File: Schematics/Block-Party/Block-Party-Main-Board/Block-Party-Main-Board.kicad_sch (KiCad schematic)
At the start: 28 parts, among them U1 ESP32-S3-DEVKITC-1-N8R2

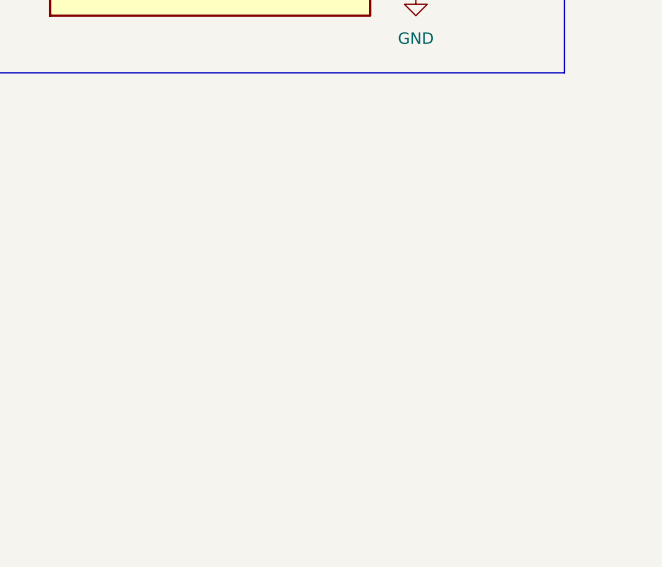
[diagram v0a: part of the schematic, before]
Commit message: Added a usb power connector.
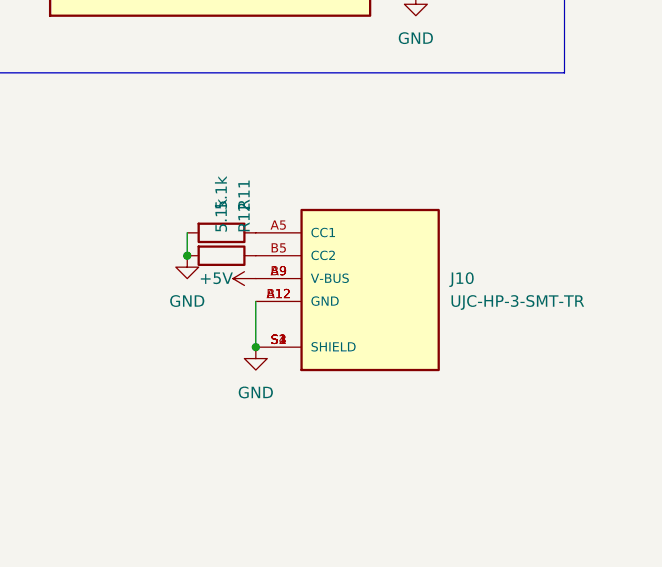
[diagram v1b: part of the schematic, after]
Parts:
- added J10: UJC-HP-3-SMT-TR, UJC-HP-3-SMT-TR:CUI_UJC-HP-3-SMT-TR, symbol UJC-HP-3-SMT-TR:UJC-HP-3-SMT-TR
- added R11, R12: 5.1k, Resistor_SMD:R_0805_2012Metric, symbol Device:R
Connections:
- net +5V: now also J10.A9 (V-BUS), J10.B9 (V-BUS)
- net GND: now also J10.A12 (GND), J10.B12 (GND), J10.S1 (SHIELD), J10.S2 (SHIELD), J10.S3 (SHIELD), J10.S4 (SHIELD), R11.2, R12.2
- new net: J10.A5 (CC1), R11.1
- new net: J10.B5 (CC2), R12.1
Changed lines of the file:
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@@
     (company "Block Party")
+  )
+  (junction (at 193.04 135.89) (diameter 0) (color 0 0 0 0)
+  )
+  (junction (at 185.42 125.73) (diameter 0) (color 0 0 0 0)
   )
   (no_connect (at 165.1 50.8))
@@
     (stroke (width 0) (type default))
   )
+  (wire (pts (xy 185.42 123.19) (xy 185.42 125.73))
+    (stroke (width 0) (type default))
+  )
+  (wire (pts (xy 193.04 130.81) (xy 193.04 135.89))
+    (stroke (width 0) (type default))
+  )
   (rectangle (start 62.23 97.79) (end 140.97 171.45)
     (stroke (width 0) (type default))
@@
     )
   )
+  (symbol (lib_id "UJC-HP-3-SMT-TR:UJC-HP-3-SMT-TR") (at 205.74 128.27 0) (unit 1)
+    (in_bom yes) (on_board yes) (dnp no) (fields_autoplaced)
+    (property "Reference" "J10" (at 214.63 128.27 0)
+      (effects (font (size 1.27 1.27)) (justify left))
+    )
+    (property "Value" "UJC-HP-3-SMT-TR" (at 214.63 130.81 0)
+      (effects (font (size 1.27 1.27)) (justify left))
+    )
+    (property "Footprint" "UJC-HP-3-SMT-TR:CUI_UJC-HP-3-SMT-TR" (at 205.74 128.27 0)
+      (effects (font (size 1.27 1.27)) (justify bottom) hide)
+    )
+    (property "Datasheet" "" (at 205.74 128.27 0)
+      (effects (font (size 1.27 1.27)) hide)
+    )
+    (property "MF" "CUI Devices" (at 205.74 128.27 0)
+      (effects (font (size 1.27 1.27)) (justify bottom) hide)
+    )
+    (property "MAXIMUM_PACKAGE_HEIGHT" "3.16mm" (at 205.74 128.27 0)
+      (effects (font (size 1.27 1.27)) (justify bottom) hide)
+    )
+    (property "Package" "Package" (at 205.74 128.27 0)
+      (effects (font (size 1.27 1.27)) (justify bottom) hide)
+    )
+    (property "Price" "None" (at 205.74 128.27 0)
+      (effects (font (size 1.27 1.27)) (justify bottom) hide)
+    )
+    (property "Check_prices" "https://www.snapeda.com/parts/UJC-HP-3-SMT-TR/CUI+Devices/view-part/?ref=eda" (at 205.74 128.27 0)
+      (effects (font (size 1.27 1.27)) (justify bottom) hide)
+    )
+    (property "STANDARD" "Manufacturer recommendations" (at 205.74 128.27 0)
+      (effects (font (size 1.27 1.27)) (justify bottom) hide)
+    )
+    (property "PARTREV" "04/30/2020" (at 205.74 128.27 0)
+      (effects (font (size 1.27 1.27)) (justify bottom) hide)
+    )
+    (property "SnapEDA_Link" "https://www.snapeda.com/parts/UJC-HP-3-SMT-TR/CUI+Devices/view-part/?ref=snap" (at 205.74 128.27 0)
+      (effects (font (size 1.27 1.27)) (justify bottom) hide)
+    )
+    (property "MP" "UJC-HP-3-SMT-TR" (at 205.74 128.27 0)
+      (effects (font (size 1.27 1.27)) (justify bottom) hide)
+    )
+    (property "Purchase-URL" "https://www.snapeda.com/api/url_track_click_mouser/?unipart_id=4722774&manufacturer=CUI Devices&part_name=UJC-HP-3-SMT-TR&search_term=usb c" (at 205.74 128.27 0)
+      (effects (font (size 1.27 1.27)) (justify bottom) hide)
+    )
+    (property "Description" "Type C, 20 Vdc, 3 A, Right Angle, Surface Mount, Black Insulator, Power-Only USB Receptacle" (at 205.74 128.27 0)
+      (effects (font (size 1.27 1.27)) (justify bottom) hide)
+    )
+    (property "CUI_purchase_URL" "https://www.cuidevices.com/product/interconnect/connectors/usb-connectors/ujc-hp-3-smt-tr?utm_source=snapeda.com&utm_medium=referral&utm_campaign=snapedaBOM" (at 205.74 128.27 0)
+      (effects (font (size 1.27 1.27)) (justify bottom) hide)
+    )
+    (property "Availability" "In Stock" (at 205.74 128.27 0)
+      (effects (font (size 1.27 1.27)) (justify bottom) hide)
+    )
+    (property "MANUFACTURER" "CUI Devices" (at 205.74 128.27 0)
+      (effects (font (size 1.27 1.27)) (justify bottom) hide)
+    )
+    (pin "S2")
+    (pin "A12")
+    (pin "B9")
+    (pin "B12")
+    (pin "S4")
+    (pin "B5")
+    (pin "S1")
+    (pin "A9")
+    (pin "A5")
+    (pin "S3")
+    (instances
+      (project "Block-Party-Main-Board"
+        (path "/4100c4a7-2a4e-4286-a196-244fb7659f20"
+          (reference "J10") (unit 1)
+        )
+      )
+    )
+  )
   (symbol (lib_id "power:+5V") (at 121.92 57.15 0) (unit 1)
     (in_bom yes) (on_board yes) (dnp no) (fields_autoplaced)
@@
         (path "/4100c4a7-2a4e-4286-a196-244fb7659f20"
           (reference "#PWR014") (unit 1)
+        )
+      )
+    )
+  )
+  (symbol (lib_id "Device:R") (at 189.23 123.19 270) (unit 1)
+    (in_bom yes) (on_board yes) (dnp no)
+    (property "Reference" "R11" (at 191.77 120.65 0)
+      (effects (font (size 1.27 1.27)) (justify right))
+    )
+    (property "Value" "5.1k" (at 189.23 120.65 0)
+      (effects (font (size 1.27 1.27)) (justify right))
+    )
+    (property "Footprint" "Resistor_SMD:R_0805_2012Metric" (at 189.23 121.412 90)
+      (effects (font (size 1.27 1.27)) hide)
+    )
+    (property "Datasheet" "~" (at 189.23 123.19 0)
+      (effects (font (size 1.27 1.27)) hide)
+    )
+    (pin "1")
+    (pin "2")
+    (instances
+      (project "Block-Party-Main-Board"
+        (path "/4100c4a7-2a4e-4286-a196-244fb7659f20"
+          (reference "R11") (unit 1)
         )
       )
@@
         (path "/4100c4a7-2a4e-4286-a196-244fb7659f20"
           (reference "J4") (unit 1)
+        )
+      )
+    )
+  )
+  (symbol (lib_id "power:+5V") (at 193.04 128.27 90) (unit 1)
+    (in_bom yes) (on_board yes) (dnp no)
+    (property "Reference" "#PWR041" (at 196.85 128.27 0)
+      (effects (font (size 1.27 1.27)) hide)
+    )
+    (property "Value" "+5V" (at 190.5 128.27 90)
+      (effects (font (size 1.27 1.27)) (justify left))
+    )
+    (property "Footprint" "" (at 193.04 128.27 0)
+      (effects (font (size 1.27 1.27)) hide)
+    )
+    (property "Datasheet" "" (at 193.04 128.27 0)
+      (effects (font (size 1.27 1.27)) hide)
+    )
+    (pin "1")
+    (instances
+      (project "Block-Party-Main-Board"
+        (path "/4100c4a7-2a4e-4286-a196-244fb7659f20"
+          (reference "#PWR041") (unit 1)
+        )
+      )
+    )
+  )
+  (symbol (lib_id "Device:R") (at 189.23 125.73 270) (unit 1)
+    (in_bom yes) (on_board yes) (dnp no)
+    (property "Reference" "R12" (at 191.77 123.19 0)
+      (effects (font (size 1.27 1.27)) (justify right))
+    )
+    (property "Value" "5.1k" (at 189.23 123.19 0)
+      (effects (font (size 1.27 1.27)) (justify right))
+    )
+    (property "Footprint" "Resistor_SMD:R_0805_2012Metric" (at 189.23 123.952 90)
+      (effects (font (size 1.27 1.27)) hide)
+    )
+    (property "Datasheet" "~" (at 189.23 125.73 0)
+      (effects (font (size 1.27 1.27)) hide)
+    )
+    (pin "1")
+    (pin "2")
+    (instances
+      (project "Block-Party-Main-Board"
+        (path "/4100c4a7-2a4e-4286-a196-244fb7659f20"
+          (reference "R12") (unit 1)
         )
       )
@@
     )
   )
+  (symbol (lib_id "power:GND") (at 185.42 125.73 0) (unit 1)
+    (in_bom yes) (on_board yes) (dnp no) (fields_autoplaced)
+    (property "Reference" "#PWR043" (at 185.42 132.08 0)
+      (effects (font (size 1.27 1.27)) hide)
+    )
+    (property "Value" "GND" (at 185.42 130.81 0)
+      (effects (font (size 1.27 1.27)))
+    )
+    (property "Footprint" "" (at 185.42 125.73 0)
+      (effects (font (size 1.27 1.27)) hide)
+    )
+    (property "Datasheet" "" (at 185.42 125.73 0)
+      (effects (font (size 1.27 1.27)) hide)
+    )
+    (pin "1")
+    (instances
+      (project "Block-Party-Main-Board"
+        (path "/4100c4a7-2a4e-4286-a196-244fb7659f20"
+          (reference "#PWR043") (unit 1)
+        )
+      )
+    )
+  )
   (symbol (lib_id "Device:R") (at 97.79 132.08 90) (unit 1)
     (in_bom yes) (on_board yes) (dnp no) (fields_autoplaced)
@@
         )
       )
+    )
+  )
+  (symbol (lib_id "power:GND") (at 193.04 135.89 0) (unit 1)
+    (in_bom yes) (on_board yes) (dnp no) (fields_autoplaced)
+    (property "Reference" "#PWR040" (at 193.04 142.24 0)
+      (effects (font (size 1.27 1.27)) hide)
+    )
+    (property "Value" "GND" (at 193.04 140.97 0)
+      (effects (font (size 1.27 1.27)))
+    )
+    (property "Footprint" "" (at 193.04 135.89 0)
+      (effects (font (size 1.27 1.27)) hide)
+    )
+    (property "Datasheet" "" (at 193.04 135.89 0)
+      (effects (font (size 1.27 1.27)) hide)
+    )
+    (pin "1")
+    (instances
+      (project "Block-Party-Main-Board"
+        (path "/4100c4a7-2a4e-4286-a196-244fb7659f20"
+          (reference "#PWR040") (unit 1)
+        )
+      )

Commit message: Revision 1.01 of the PCBs
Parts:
- added J11: 691214110002S, 2p 3:691214110002S, symbol 691214110002S:691214110002S
- added TP1, TP2, TP3, TP4, TP5, TP6, TP7: TestPoint, TestPoint:TestPoint_Pad_D2.0mm, symbol Connector:TestPoint
- C1, C2, C3, C4, C5, C6, C7, C8, C9: MANUFACTURER (none) -> Samwha Capacitor; PART-NUMBER (none) -> CS2012X5R475K500NRE
- J1, J2, J3, J4, J5, J6, J7, J8, J9: now not fitted; now left out of the parts list
- J10: footprint UJC-HP-3-SMT-TR:CUI_UJC-HP-3-SMT-TR -> Quinn_lib:USB_C-0015IPX6-00; MANUFACTURER CUI Devices -> SHOU HAN; PART-NUMBER (none) -> USBC-0015IPX6-00
- R1, R2, R3, R4, R5, R6, R7, R8, R9: MANUFACTURER (none) -> Viking Tech; PART-NUMBER (none) -> AR05DTD1002
- R11, R12: MANUFACTURER (none) -> BOURNS; PART-NUMBER (none) -> CR0805-FX-5101ELF
- U1: now not fitted
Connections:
- net +5V: now also J11.1, TP2.1
- net DO1: now also TP6.1
- net DO2: now also TP7.1
- net GND: now also J11.2, TP3.1
- net SENSE1: now also TP4.1
- net SENSE2: now also TP5.1
- net at U1.J3_5 (GPIO2): now also TP1.1
- no-connect marks 18 -> 17

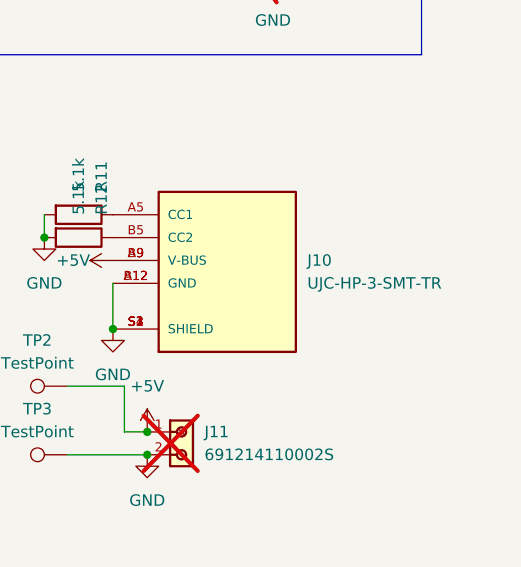
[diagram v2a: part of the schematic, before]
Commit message: Found a good jst part number and updated the BOMs
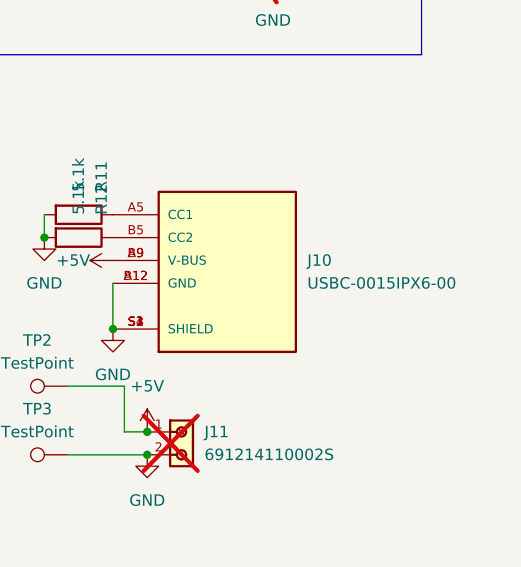
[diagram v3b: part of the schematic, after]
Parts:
- J10: value UJC-HP-3-SMT-TR -> USBC-0015IPX6-00
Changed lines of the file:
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@@
 			)
 		)
-		(property "Value" "UJC-HP-3-SMT-TR"
+		(property "Value" "USBC-0015IPX6-00"
 			(at 214.63 130.81 0)
 			(effects
